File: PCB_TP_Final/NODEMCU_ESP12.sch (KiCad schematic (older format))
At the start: 1 part, among them U1 NODEMCU_ESP12

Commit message: Primera entrega (1.0) para revision
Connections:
- net +3V3: now reaches U1.16 (3V16)
- net HCS: now reaches U1.20 (D8)
- net HMOSI: now reaches U1.21 (D7)
- net HMISO: now reaches U1.22 (D6)
- net HSCLK: now reaches U1.23 (D5)
- no-connect marks 29 -> 24
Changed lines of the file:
@@
 LIBS:valves
 LIBS:nodemcu_esp12
+LIBS:power_mb_v2
 LIBS:PCB_TP_Final-cache
 EELAYER 25 0
@@
 $Descr A4 11693 8268
 encoding utf-8
-Sheet 3 3
+Sheet 3 4
 Title ""
-Date ""
+Date "2018-09-26"
 Rev ""
 Comp ""
@@
 NoConn ~ 6100 2550
 NoConn ~ 6200 2550
-NoConn ~ 6300 2550
 NoConn ~ 6400 2550
 NoConn ~ 5550 2800
@@
 NoConn ~ 6300 4050
 NoConn ~ 6500 4050
-NoConn ~ 7150 3800
-NoConn ~ 7150 3700
-NoConn ~ 7150 3600
-NoConn ~ 7150 3500
 NoConn ~ 7150 3400
 NoConn ~ 7150 3300
@@
 NoConn ~ 7150 2800
 $Comp
-L GND #PWR05
+L GND #PWR03
 U 1 1 5BA67FB6
 P 6400 4300
-F 0 "#PWR05" H 6400 4050 50  0001 C CNN
+F 0 "#PWR03" H 6400 4050 50  0001 C CNN
 F 1 "GND" H 6400 4150 50  0000 C CNN
 F 2 "" H 6400 4300 50  0001 C CNN
@@
 Wire Wire Line
 	6400 4050 6400 4300
+$Comp
+L +3V3 #PWR04
+U 1 1 5BA9BFC5
+P 6300 2350
+F 0 "#PWR04" H 6300 2200 50  0001 C CNN
+F 1 "+3V3" H 6300 2490 50  0000 C CNN
+F 2 "" H 6300 2350 50  0001 C CNN
+F 3 "" H 6300 2350 50  0001 C CNN
+	1    6300 2350
+	1    0    0    -1
+$EndComp
+Wire Wire Line
+	6300 2550 6300 2350
+Text HLabel 7350 3500 2    60   Input ~ 0
+HSCLK
+Text HLabel 7350 3600 2    60   Input ~ 0
+HMISO
+Text HLabel 7350 3700 2    60   Input ~ 0
+HMOSI
+Text HLabel 7350 3800 2    60   Input ~ 0
+HCS
+Wire Wire Line
+	7150 3500 7350 3500
+Wire Wire Line
+	7150 3600 7350 3600
+Wire Wire Line
+	7150 3700 7350 3700
+Wire Wire Line
+	7150 3800 7350 3800
 $EndSCHEMATC

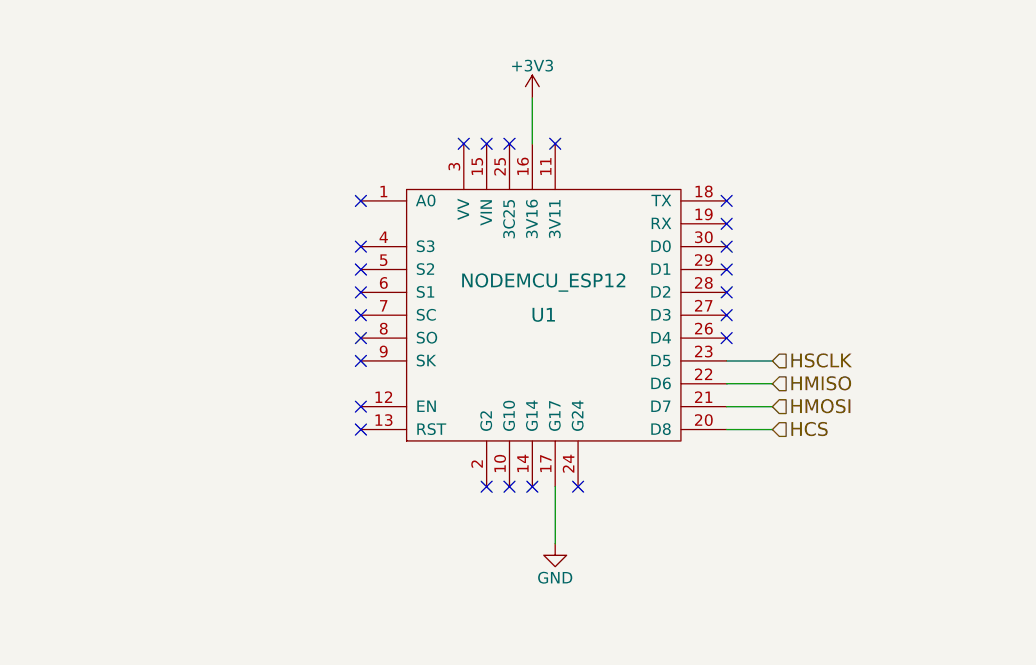
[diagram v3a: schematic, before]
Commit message: Se agregaron correcciones sugeridas
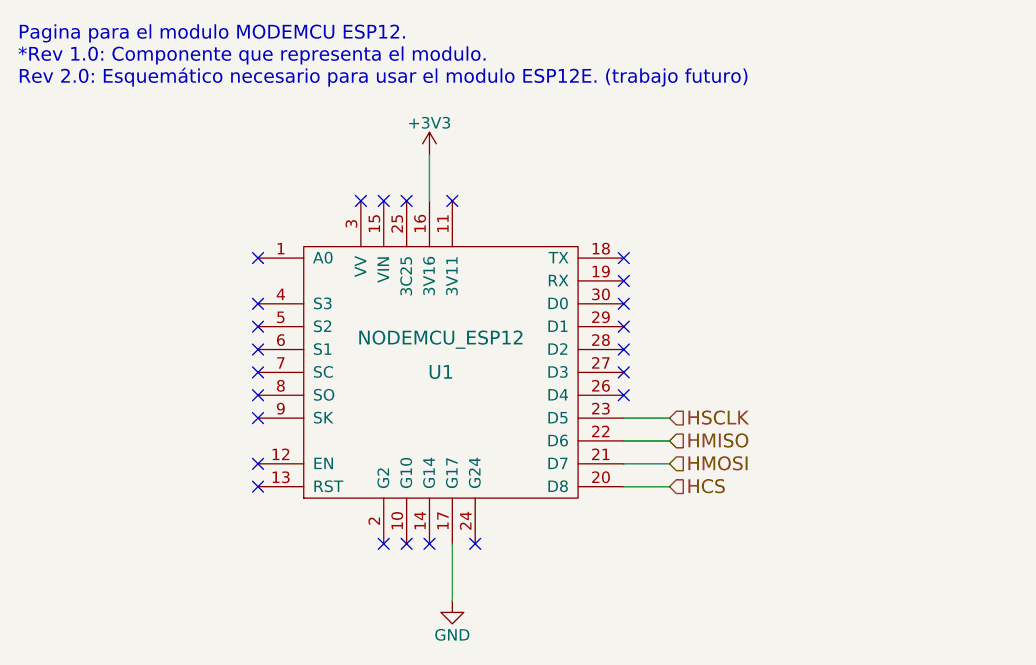
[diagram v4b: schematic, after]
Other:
- note added: "Pagina para el modulo MODEMCU ESP12.\n*Rev 1.0: Componente que representa el modulo.\nRev 2.0: Esquemático necesario para usar el modulo ESP12E. (trabajo futuro)"
- moved on the sheet: U1
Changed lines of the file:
@@
 encoding utf-8
 Sheet 3 5
-Title ""
+Title "NodeMCU ESP12"
 Date "2018-09-26"
-Rev ""
-Comp ""
+Rev "1.0"
+Comp "Ericson Joseph Estupiñan Pineda"
 Comment1 ""
 Comment2 ""
@@
 L NODEMCU_ESP12 U1
 U 1 1 5BA67E06
-P 6350 3300
-F 0 "U1" H 6350 3300 60  0000 C CNN
-F 1 "NODEMCU_ESP12" H 6350 3450 60  0000 C CNN
-F 2 "NODEMCU_ESP12:NODEMCU_ESP12" H 6350 3300 60  0001 C CNN
-F 3 "" H 6350 3300 60  0001 C CNN
-	1    6350 3300
+P 5900 3550
+F 0 "U1" H 5900 3550 60  0000 C CNN
+F 1 "NODEMCU_ESP12" H 5900 3700 60  0000 C CNN
+F 2 "NODEMCU_ESP12:NODEMCU_ESP12" H 5900 3550 60  0001 C CNN
+F 3 "" H 5900 3550 60  0001 C CNN
+	1    5900 3550
 	1    0    0    -1
 $EndComp
-NoConn ~ 6000 2550
-NoConn ~ 6100 2550
-NoConn ~ 6200 2550
-NoConn ~ 6400 2550
 NoConn ~ 5550 2800
-NoConn ~ 5550 3000
-NoConn ~ 5550 3100
-NoConn ~ 5550 3200
-NoConn ~ 5550 3300
-NoConn ~ 5550 3400
-NoConn ~ 5550 3500
-NoConn ~ 5550 3700
-NoConn ~ 5550 3800
-NoConn ~ 6100 4050
-NoConn ~ 6200 4050
-NoConn ~ 6300 4050
-NoConn ~ 6500 4050
-NoConn ~ 7150 3400
-NoConn ~ 7150 3300
-NoConn ~ 7150 3200
-NoConn ~ 7150 3100
-NoConn ~ 7150 3000
-NoConn ~ 7150 2900
-NoConn ~ 7150 2800
+NoConn ~ 5650 2800
+NoConn ~ 5750 2800
+NoConn ~ 5950 2800
+NoConn ~ 5100 3050
+NoConn ~ 5100 3250
+NoConn ~ 5100 3350
+NoConn ~ 5100 3450
+NoConn ~ 5100 3550
+NoConn ~ 5100 3650
+NoConn ~ 5100 3750
+NoConn ~ 5100 3950
+NoConn ~ 5100 4050
+NoConn ~ 5650 4300
+NoConn ~ 5750 4300
+NoConn ~ 5850 4300
+NoConn ~ 6050 4300
+NoConn ~ 6700 3650
+NoConn ~ 6700 3550
+NoConn ~ 6700 3450
+NoConn ~ 6700 3350
+NoConn ~ 6700 3250
+NoConn ~ 6700 3150
+NoConn ~ 6700 3050
 $Comp
-L GND #PWR04
+L GND #PWR07
 U 1 1 5BA67FB6
-P 6400 4300
-F 0 "#PWR04" H 6400 4050 50  0001 C CNN
-F 1 "GND" H 6400 4150 50  0000 C CNN
-F 2 "" H 6400 4300 50  0001 C CNN
-F 3 "" H 6400 4300 50  0001 C CNN
-	1    6400 4300
+P 5950 4550
+F 0 "#PWR07" H 5950 4300 50  0001 C CNN
+F 1 "GND" H 5950 4400 50  0000 C CNN
+F 2 "" H 5950 4550 50  0001 C CNN
+F 3 "" H 5950 4550 50  0001 C CNN
+	1    5950 4550
 	1    0    0    -1
 $EndComp
 Wire Wire Line
-	6400 4050 6400 4300
+	5950 4300 5950 4550
 $Comp
-L +3V3 #PWR05
+L +3V3 #PWR08
 U 1 1 5BA9BFC5
-P 6300 2350
-F 0 "#PWR05" H 6300 2200 50  0001 C CNN
-F 1 "+3V3" H 6300 2490 50  0000 C CNN
-F 2 "" H 6300 2350 50  0001 C CNN
-F 3 "" H 6300 2350 50  0001 C CNN
-	1    6300 2350
+P 5850 2600
+F 0 "#PWR08" H 5850 2450 50  0001 C CNN
+F 1 "+3V3" H 5850 2740 50  0000 C CNN
+F 2 "" H 5850 2600 50  0001 C CNN
+F 3 "" H 5850 2600 50  0001 C CNN
+	1    5850 2600
 	1    0    0    -1
 $EndComp
 Wire Wire Line
-	6300 2550 6300 2350
-Text HLabel 7350 3500 2    60   Input ~ 0
+	5850 2800 5850 2600
+Text HLabel 6900 3750 2    60   Input ~ 0
 HSCLK
-Text HLabel 7350 3600 2    60   Input ~ 0
+Text HLabel 6900 3850 2    60   Input ~ 0
 HMISO
-Text HLabel 7350 3700 2    60   Input ~ 0
+Text HLabel 6900 3950 2    60   Input ~ 0
 HMOSI
-Text HLabel 7350 3800 2    60   Input ~ 0
+Text HLabel 6900 4050 2    60   Input ~ 0
 HCS
 Wire Wire Line
-	7150 3500 7350 3500
+	6700 3750 6900 3750
 Wire Wire Line
-	7150 3600 7350 3600
+	6700 3850 6900 3850
 Wire Wire Line
-	7150 3700 7350 3700
+	6700 3950 6900 3950
 Wire Wire Line
-	7150 3800 7350 3800
+	6700 4050 6900 4050
+Text Notes 4050 2300 0    60   ~ 0
+Pagina para el modulo MODEMCU ESP12.\n*Rev 1.0: Componente que representa el modulo.\nRev 2.0: Esquemático necesario para usar el modulo ESP12E. (trabajo futuro)
 $EndSCHEMATC

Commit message: para fabricar
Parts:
- added R5: 10K, Resistors_SMD:R_1206_HandSoldering, symbol R
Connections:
- wire segments 6 -> 9
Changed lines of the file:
@@
 	1    0    0    -1
 $EndComp
-Wire Wire Line
-	5950 4300 5950 4550
 $Comp
 L +3V3 #PWR08
@@
 	1    0    0    -1
 $EndComp
-Wire Wire Line
-	5850 2800 5850 2600
 Text HLabel 6900 3750 2    60   Input ~ 0
 HSCLK
 Text HLabel 6900 3850 2    60   Input ~ 0
 HMISO
-Text HLabel 6900 3950 2    60   Input ~ 0
+Text HLabel 7470 3950 2    60   Input ~ 0
 HMOSI
 Text HLabel 6900 4050 2    60   Input ~ 0
 HCS
+Text Notes 4050 2300 0    60   ~ 0
+Pagina para el modulo MODEMCU ESP12.\n*Rev 1.0: Componente que representa el modulo.\nRev 2.0: Esquemático necesario para usar el modulo ESP12E. (trabajo futuro)
+$Comp
+L R R5
+U 1 1 5BEA4DE2
+P 7310 4280
+F 0 "R5" V 7390 4280 50  0000 C CNN
+F 1 "10K" V 7310 4280 50  0000 C CNN
+F 2 "Resistors_SMD:R_1206_HandSoldering" V 7240 4280 50  0001 C CNN
+F 3 "" H 7310 4280 50  0001 C CNN
+	1    7310 4280
+	1    0    0    -1
+$EndComp
+Connection ~ 5950 4490
+Wire Wire Line
+	7310 4490 5950 4490
+Wire Wire Line
+	7310 4440 7310 4490
+Connection ~ 7310 3950
+Wire Wire Line
+	7310 4130 7310 3950
+Wire Wire Line
+	6700 3950 7470 3950
+Wire Wire Line
+	6700 4050 6900 4050
+Wire Wire Line
+	6700 3850 6900 3850
 Wire Wire Line
 	6700 3750 6900 3750
 Wire Wire Line
-	6700 3850 6900 3850
+	5850 2800 5850 2600
 Wire Wire Line
-	6700 3950 6900 3950
-Wire Wire Line
-	6700 4050 6900 4050
-Text Notes 4050 2300 0    60   ~ 0
-Pagina para el modulo MODEMCU ESP12.\n*Rev 1.0: Componente que representa el modulo.\nRev 2.0: Esquemático necesario para usar el modulo ESP12E. (trabajo futuro)
+	5950 4300 5950 4550
 $EndSCHEMATC
